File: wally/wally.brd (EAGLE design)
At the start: 41 x 101 mm, 94 parts, among them IC1 ESP32-S3-WROOM-1U-N16, IC2 XTLV61048DBVR, IC3 TLV1117LV33DCYR, IC4 DPS310XTSA1, IC5 BMI323, IC6 MCP96L00T-E_MX, IC7 MLX90395KLW-BBA-001-SP, J1 MSD-4-A, J2 QWIIC_RIGHT_ANGLE, J3 QWIIC_RIGHT_ANGLE, J4 S2B-PH-K-S(LF)(SN), J6 USBC, U1 RA-01H

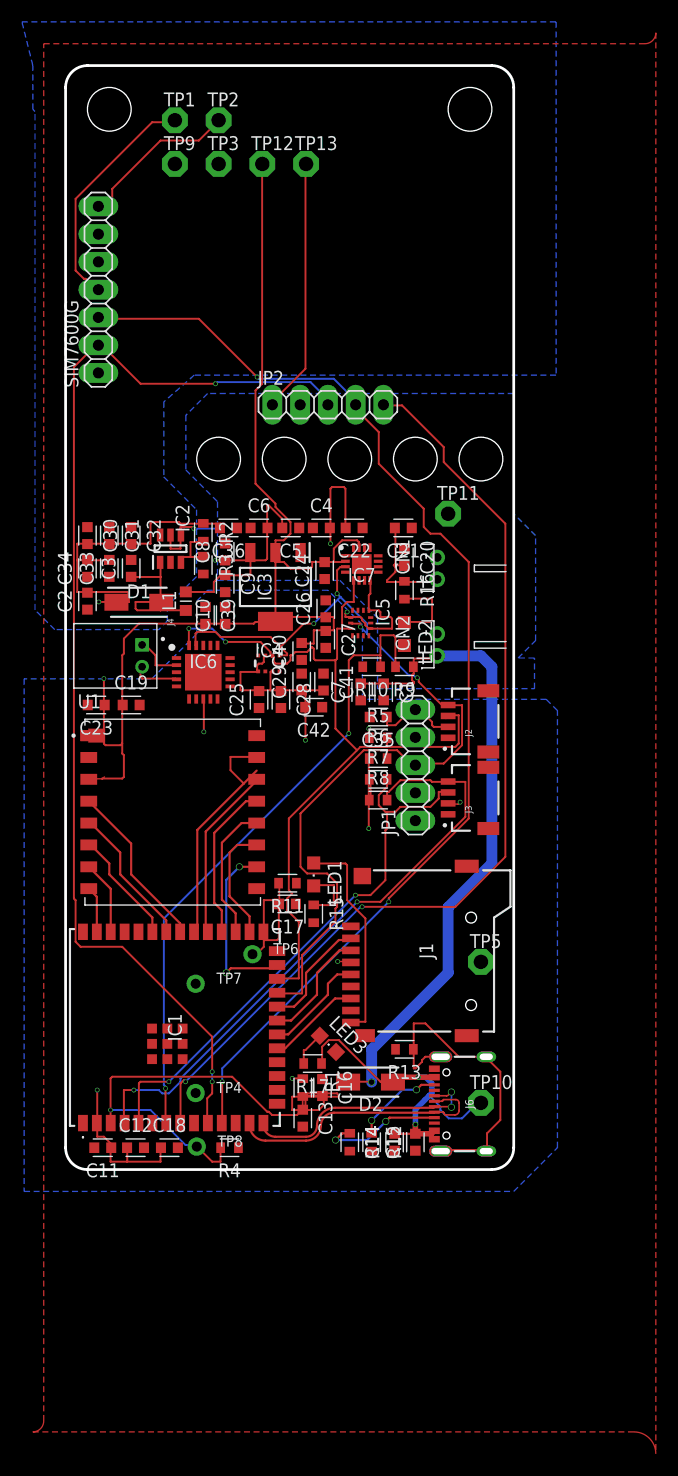
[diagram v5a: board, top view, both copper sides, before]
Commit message: add some status LEDs
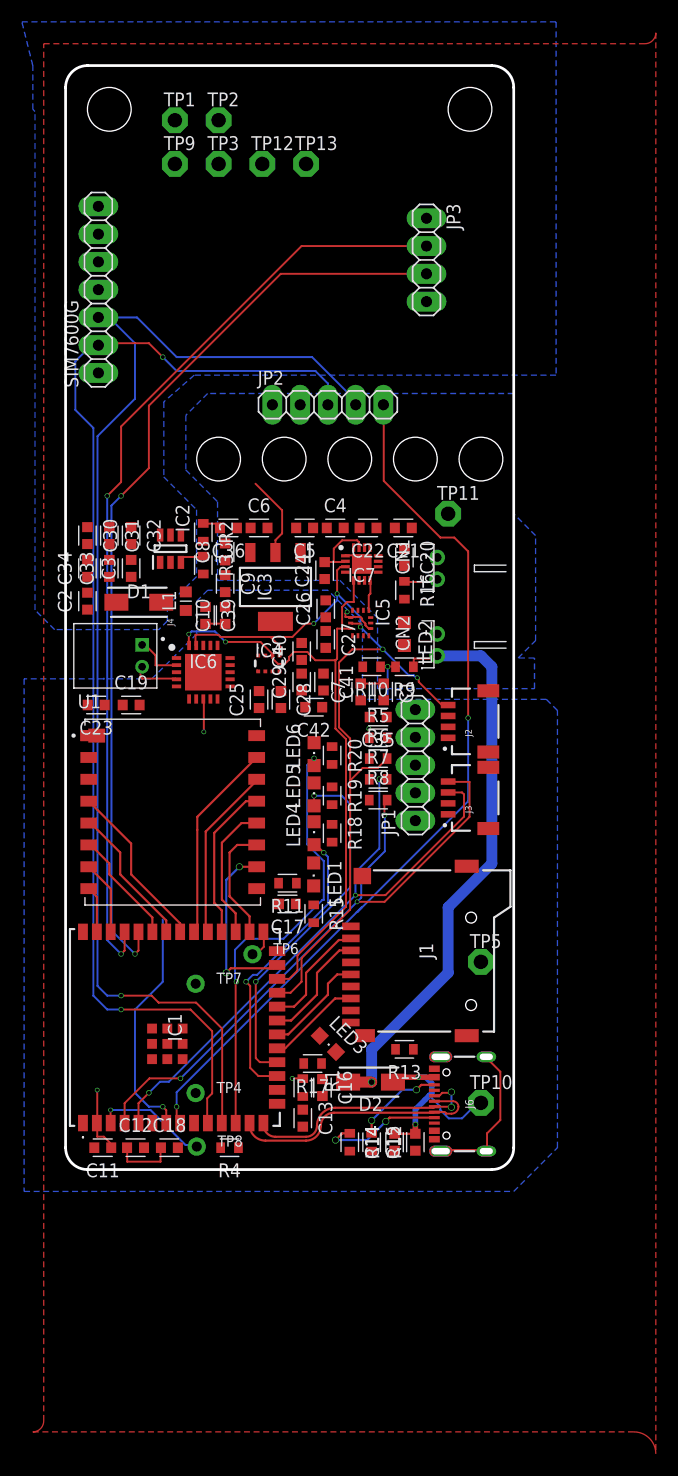
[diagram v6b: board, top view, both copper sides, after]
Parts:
- added JP3: PINHD-1X4, Connector:1X04
- added LED4, LED5: LEDG, adafruit:CHIPLED_0805
- added LED6: LEDR, adafruit:CHIPLED_0805
- added R18, R19: 33, Resistor:RESC1608X60
- added R20: 51, Resistor:RESC1608X60
- LED1: value (none) -> LEDG
- LED2: value (none) -> LEDW
- LED3: value (none) -> LEDY
- R17: value 5k1 -> 150
- moved C22 1.27 mm to (27.7, -42.3)
- moved C4 1.27 mm to (24.7, -42.3)
- moved C5 1.27 mm to (21.9, -42.3)
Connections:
- new net ERR_LED: IC1.12, LED6.A
- new net LTE_STATUS: IC1.17, LED4.A
- new net N$11: LED6.C, R20.1
- new net N$7: LED4.C, R18.1
- new net N$8: LED5.C, R19.1
- new net RAD_STATUS: IC1.18, LED5.A
- new net RX0: IC1.36, JP3.3
- new net TX0: IC1.37, JP3.2
- net 3V3: now also JP3.1
- net GND: now also JP3.4, R18.2, R19.2, R20.2
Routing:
- net 3V3: track 181.8 -> 44.1 mm, vias 10 -> 5
- net TX0: track 0.00 -> 86.3 mm, vias 0 -> 2
- net RX0: track 0.00 -> 85.0 mm, vias 0 -> 2
- net VCC: track 135.7 -> 61.2 mm, vias 4 -> 1
- net EN: track 54.0 -> 11.4 mm
- net ERR_LED: track 0.00 -> 40.9 mm, vias 0 -> 2
- net VSENSE: track 59.6 -> 26.0 mm
- net RAD_STATUS: track 0.00 -> 33.5 mm, vias 0 -> 2
- net VSIM: track 31.3 -> 3.22 mm, vias 1 -> 0
- net LTE_STATUS: track 0.00 -> 27.3 mm, vias 0 -> 2
- net PWRKEY: track 22.4 -> 0.00 mm
- net N$49: track 21.1 -> 0.05 mm
- net SDA0: track 80.4 -> 60.5 mm
- net SLEEP: track 18.0 -> 0.43 mm
- net N$2: track 15.3 -> 0.61 mm
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
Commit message: fix all airwires
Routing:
- net 3V3: track 44.1 -> 160.7 mm, vias 5 -> 30
- net VCC: track 61.2 -> 131.4 mm, vias 1 -> 22
- net VSENSE: track 26.0 -> 59.5 mm
- net GND: track 2.93 -> 30.3 mm, vias 0 -> 6
- net N$49: track 0.05 -> 24.4 mm, vias 0 -> 4
- net PWRKEY: track 0.00 -> 21.6 mm, vias 0 -> 2
- net VSIM: track 3.22 -> 24.1 mm, vias 0 -> 7
- net EN: track 11.4 -> 30.4 mm, vias 1 -> 2
- net SDA0: track 60.5 -> 75.4 mm, vias 2 -> 3
- net SLEEP: track 0.43 -> 14.8 mm
- net VBUS: track 18.9 -> 28.3 mm
- net N$2: track 0.61 -> 9.54 mm
- net N$21: track 14.8 -> 21.7 mm
- net BOOT: track 2.60 -> 7.90 mm
- net N$4: track 0.14 -> 3.17 mm
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
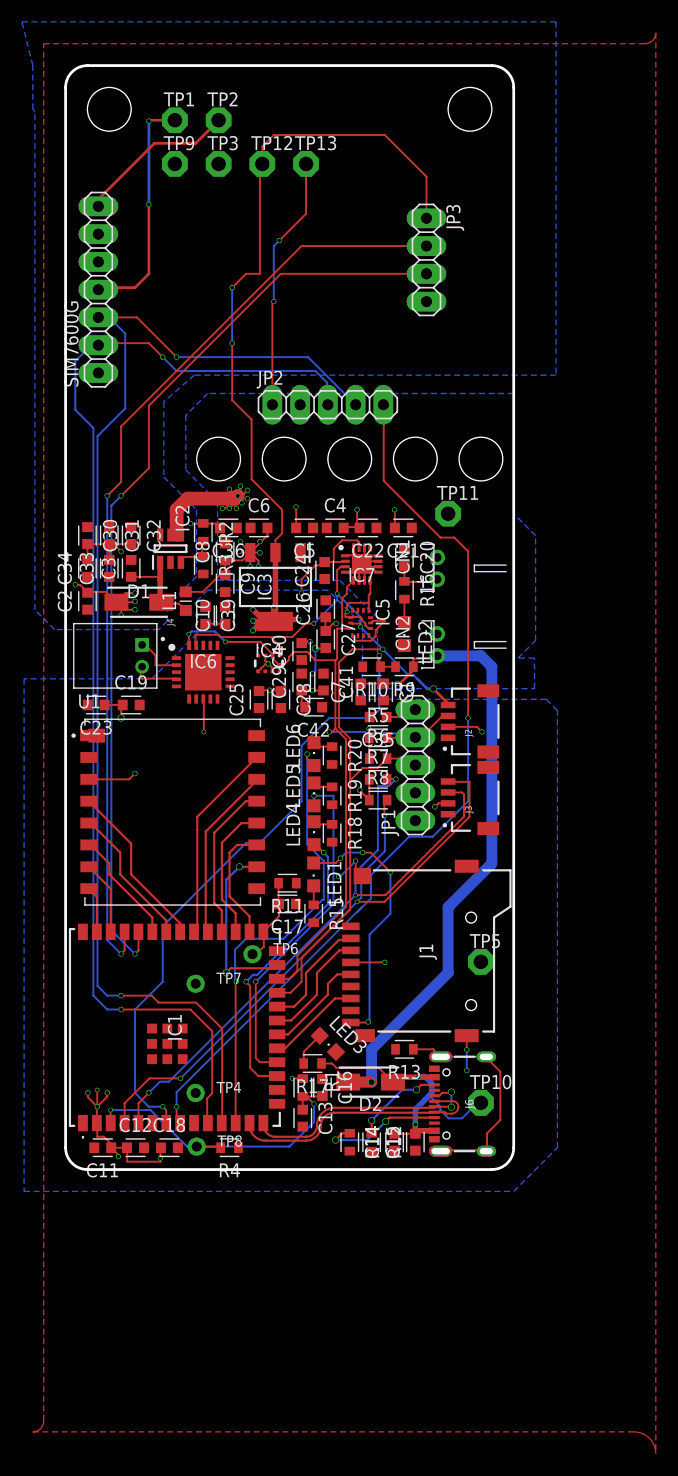
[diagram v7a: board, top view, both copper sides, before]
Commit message: delete wire stubs
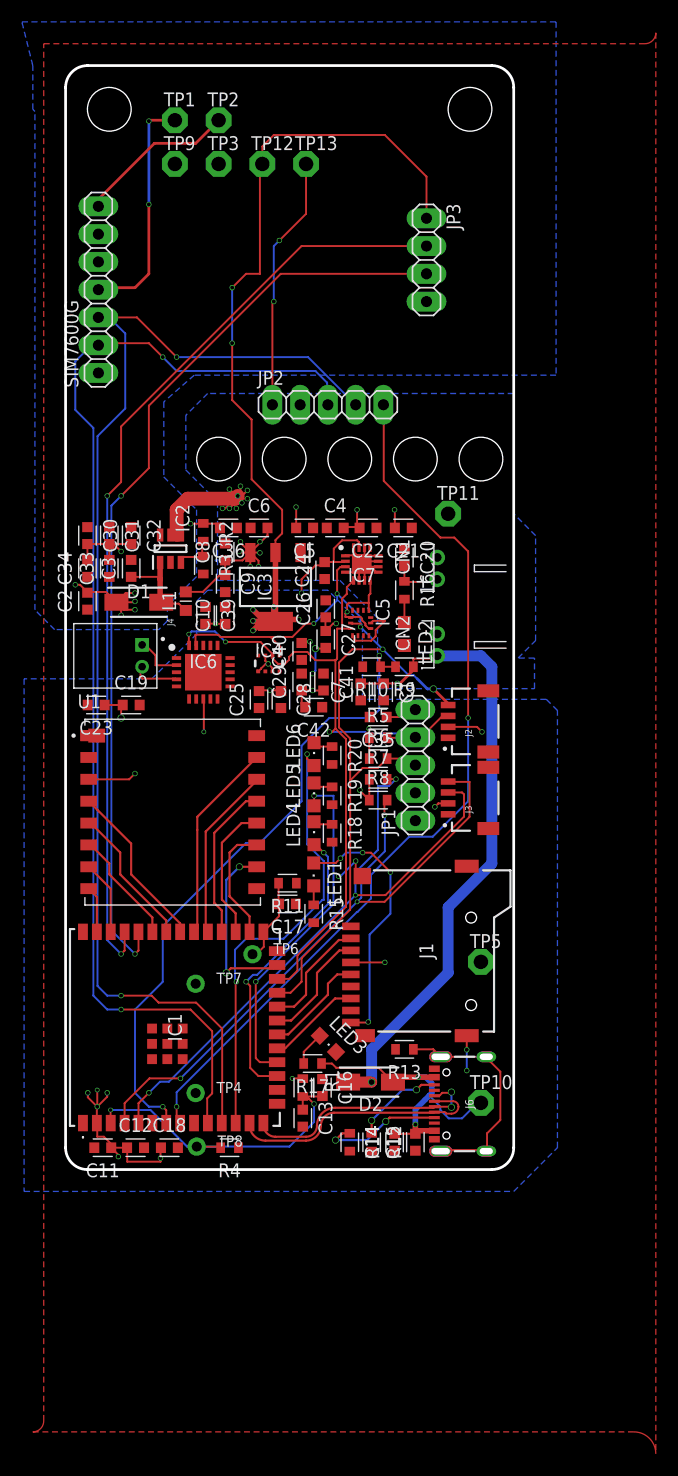
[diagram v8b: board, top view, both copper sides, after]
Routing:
- net SDA0: track 75.4 -> 74.2 mm
- net N$21: track 21.7 -> 21.0 mm
- net PPS: track 82.8 -> 82.1 mm
- net SDA1: track 60.4 -> 59.8 mm
- net SD_CS: track 11.0 -> 10.5 mm
